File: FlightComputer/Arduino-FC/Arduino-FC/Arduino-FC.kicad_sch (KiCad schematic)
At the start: 5 parts, among them J1 Conn_02x04_Counter_Clockwise, J2 Conn_01x06, J3 Conn_01x07, J4 Conn_01x05, U1 TPS61236PRWLR

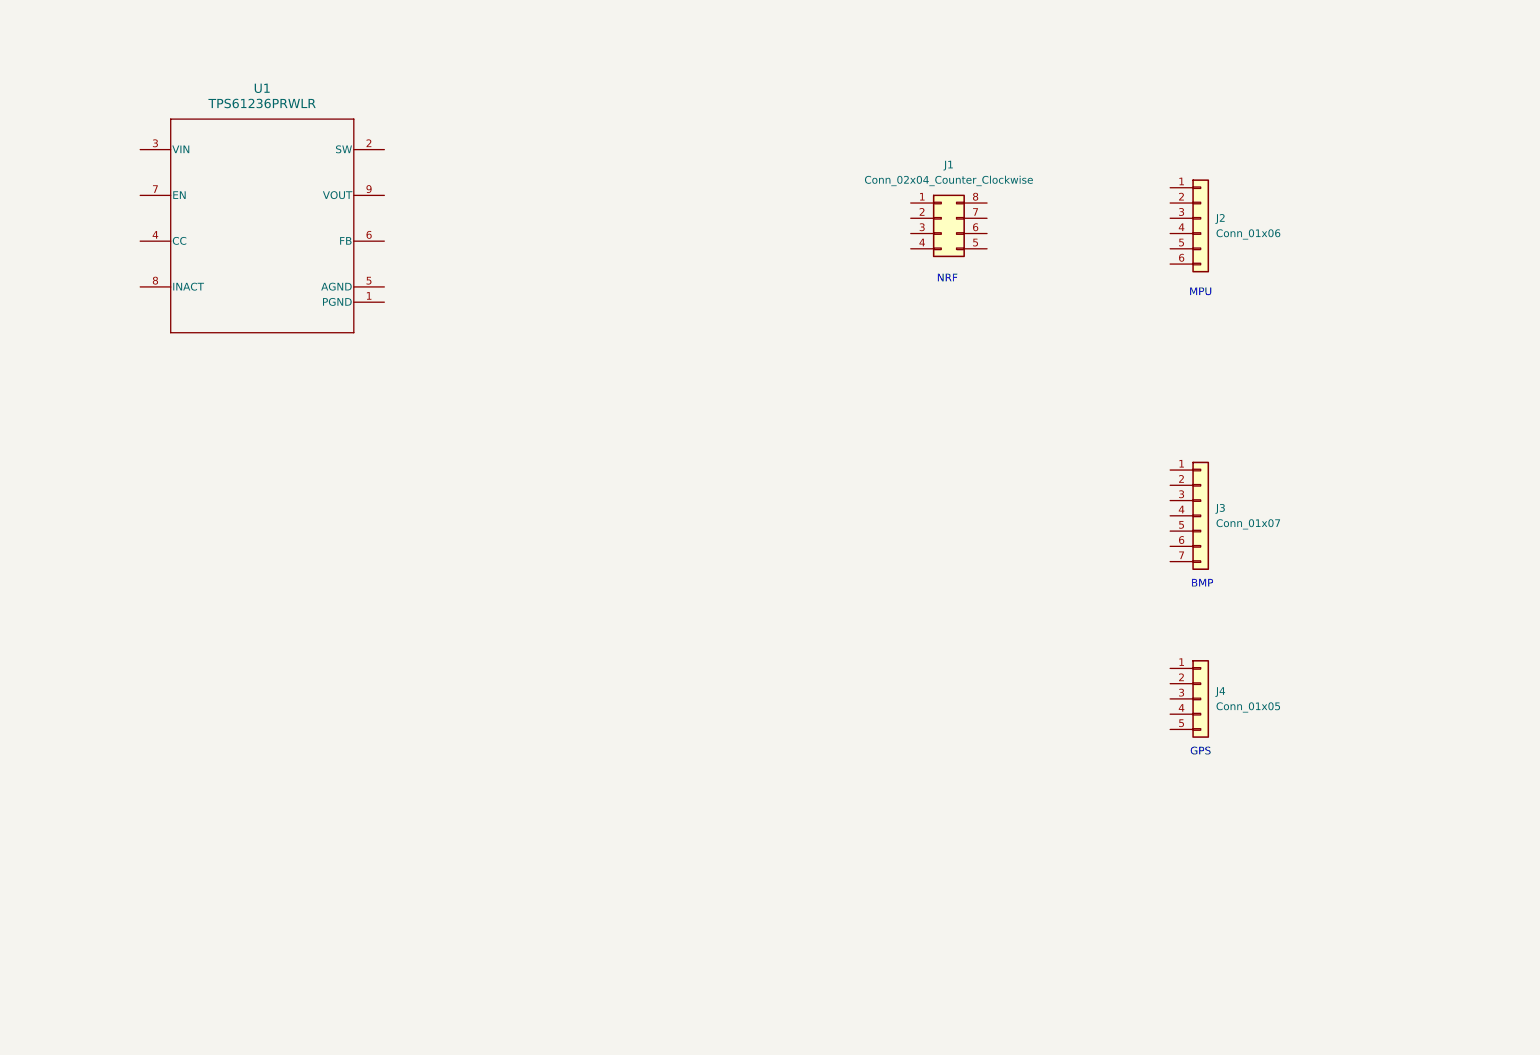
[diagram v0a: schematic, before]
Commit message: Added Main.ino
Updated schematic connections
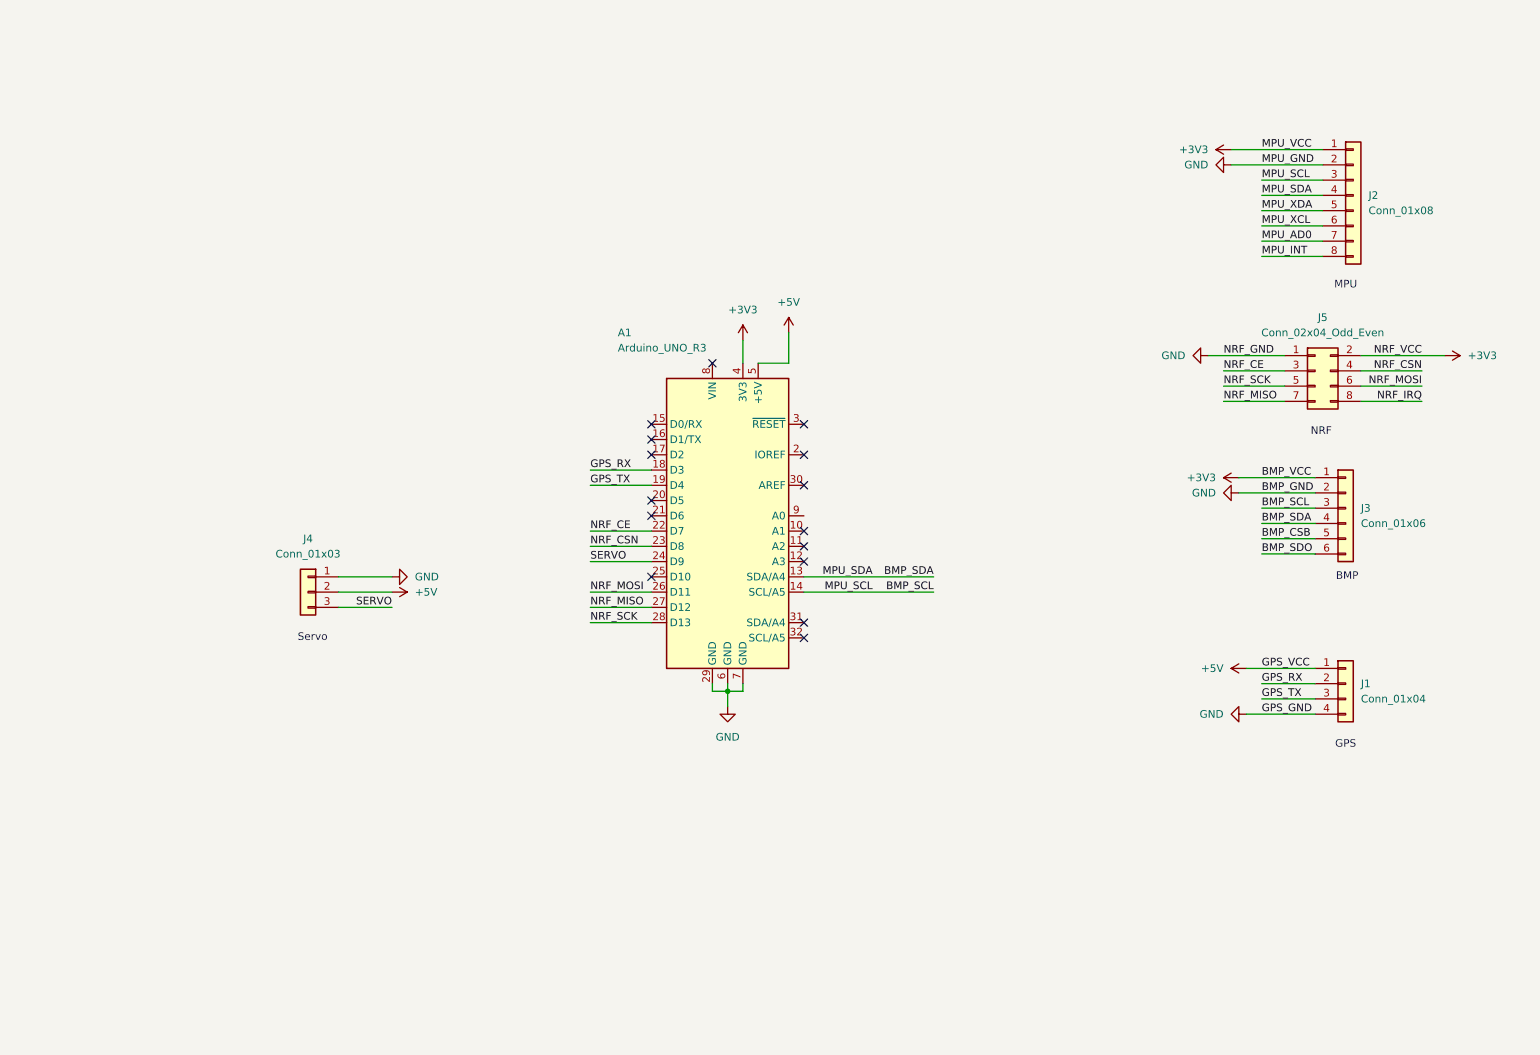
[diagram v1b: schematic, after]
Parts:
- removed J1: Conn_02x04_Counter_Clockwise, symbol Connector_Generic:Conn_02x04_Counter_Clockwise
- removed J2: Conn_01x06, symbol Connector_Generic:Conn_01x06
- removed J3: Conn_01x07, symbol Connector_Generic:Conn_01x07
- removed J4: Conn_01x05, symbol Connector_Generic:Conn_01x05
- removed U1: TPS61236PRWLR, RWL0009A, symbol TPS61236P:TPS61236PRWLR
- added A1: Arduino_UNO_R3, Module:Arduino_UNO_R3, symbol MCU_Module:Arduino_UNO_R3
- added J1: Conn_01x04, symbol Connector_Generic:Conn_01x04
- added J2: Conn_01x08, symbol Connector_Generic:Conn_01x08
- added J3: Conn_01x06, symbol Connector_Generic:Conn_01x06
- added J4: Conn_01x03, symbol Connector_Generic:Conn_01x03
- added J5: Conn_02x04_Odd_Even, symbol Connector_Generic:Conn_02x04_Odd_Even
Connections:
- new net +3V3: A1.4 (3V3), J2.1 (Pin_1), J3.1 (Pin_1), J5.2 (Pin_2)
- new net +5V: A1.5 (+5V), J1.1 (Pin_1), J4.2 (Pin_2)
- new net BMP_CSB: J3.5 (Pin_5)
- new net BMP_SCL: A1.14 (SCL/A5), J2.3 (Pin_3), J3.3 (Pin_3)
- new net BMP_SDA: A1.13 (SDA/A4), J2.4 (Pin_4), J3.4 (Pin_4)
- new net BMP_SDO: J3.6 (Pin_6)
- new net GND: A1.29 (GND), A1.6 (GND), A1.7 (GND), J1.4 (Pin_4), J2.2 (Pin_2), J3.2 (Pin_2), J4.1 (Pin_1), J5.1 (Pin_1)
- new net GPS_RX: A1.18 (D3), J1.2 (Pin_2)
- new net GPS_TX: A1.19 (D4), J1.3 (Pin_3)
- new net MPU_AD0: J2.7 (Pin_7)
- new net MPU_INT: J2.8 (Pin_8)
- new net MPU_XCL: J2.6 (Pin_6)
- new net MPU_XDA: J2.5 (Pin_5)
- new net NRF_CE: A1.22 (D7), J5.3 (Pin_3)
- new net NRF_CSN: A1.23 (D8), J5.4 (Pin_4)
- new net NRF_IRQ: J5.8 (Pin_8)
- new net NRF_MISO: A1.27 (D12), J5.7 (Pin_7)
- new net NRF_MOSI: A1.26 (D11), J5.6 (Pin_6)
- new net NRF_SCK: A1.28 (D13), J5.5 (Pin_5)
- new net SERVO: A1.24 (D9), J4.3 (Pin_3)
- no-connect marks 0 -> 15
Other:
- note added: "Servo"

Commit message: Buck Converter
Footprint assignments
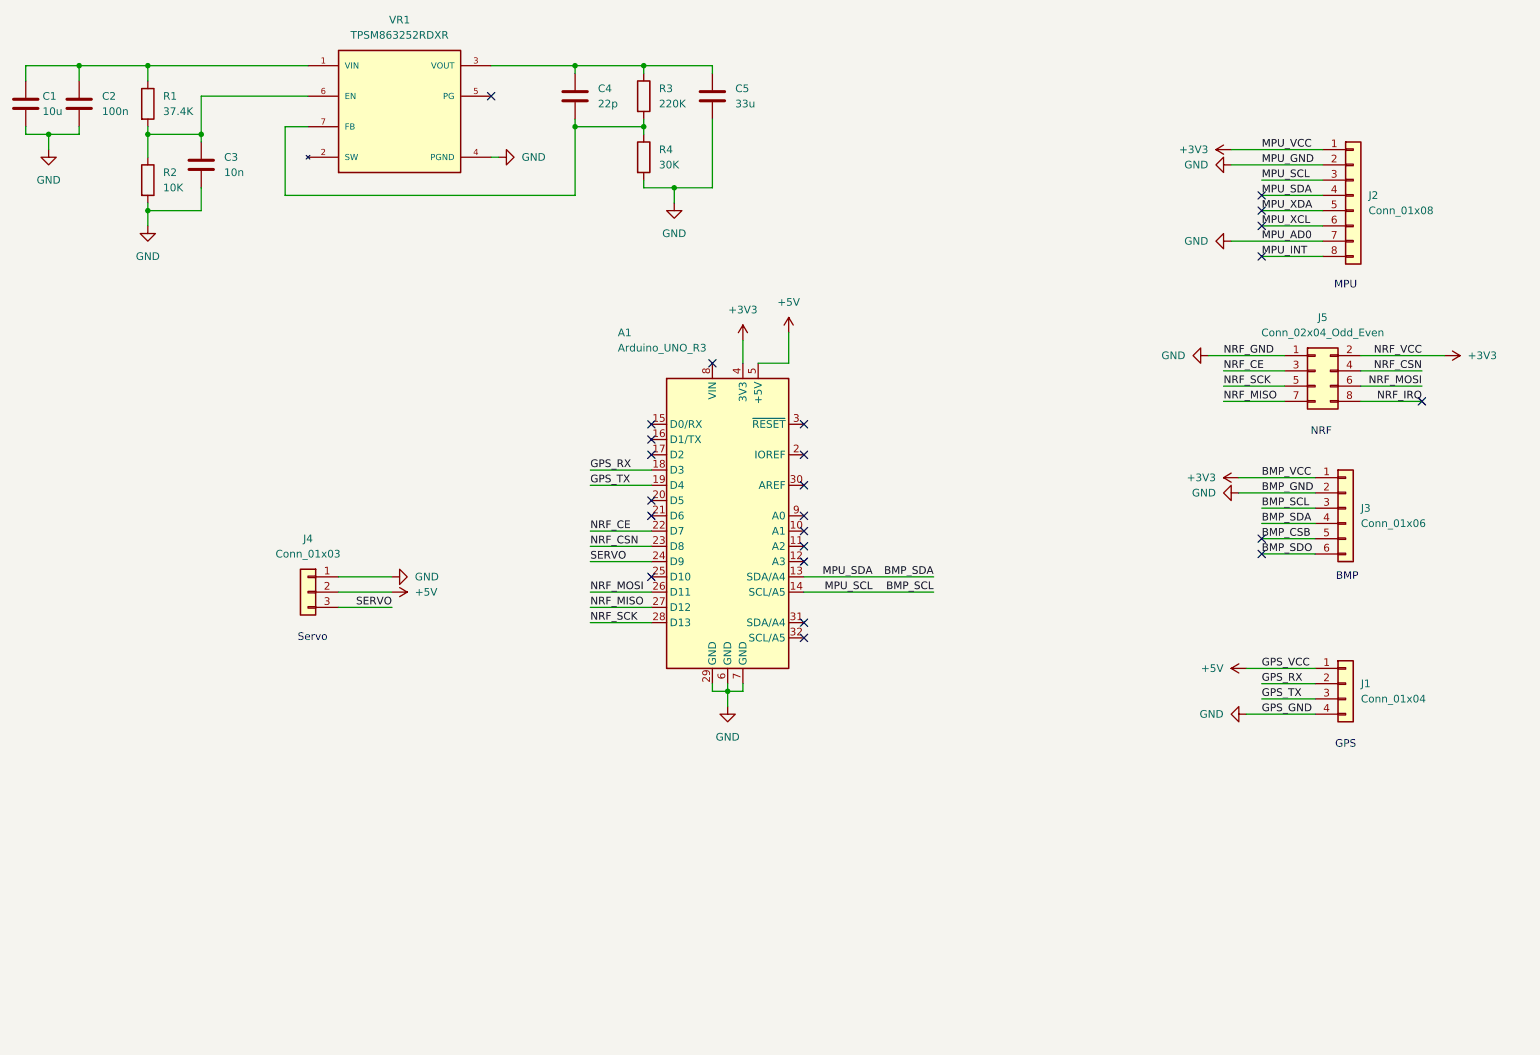
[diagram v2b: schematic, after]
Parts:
- added C1: 10u, Capacitor_SMD:C_0805_2012Metric_Pad1.18x1.45mm_HandSolder, symbol Device:C
- added C2: 100n, Capacitor_SMD:C_0402_1005Metric_Pad0.74x0.62mm_HandSolder, symbol Device:C
- added C3: 10n, Capacitor_SMD:C_0402_1005Metric_Pad0.74x0.62mm_HandSolder, symbol Device:C
- added C4: 22p, Capacitor_SMD:C_0402_1005Metric_Pad0.74x0.62mm_HandSolder, symbol Device:C
- added C5: 33u, Capacitor_SMD:C_1812_4532Metric_Pad1.57x3.40mm_HandSolder, symbol Device:C
- added R1: 37.4K, Resistor_SMD:R_0402_1005Metric_Pad0.72x0.64mm_HandSolder, symbol Device:R
- added R2: 10K, Resistor_SMD:R_0402_1005Metric_Pad0.72x0.64mm_HandSolder, symbol Device:R
- added R3: 220K, Resistor_SMD:R_0603_1608Metric_Pad0.98x0.95mm_HandSolder, symbol Device:R
- added R4: 30K, Resistor_SMD:R_0603_1608Metric_Pad0.98x0.95mm_HandSolder, symbol Device:R
- added VR1: TPSM863252RDXR, TPSM863252RDXR:VREG_TPSM863252RDXR, symbol TPSM863252RDXR:TPSM863252RDXR
- J1: footprint (none) -> Connector_PinHeader_2.54mm:PinHeader_1x04_P2.54mm_Vertical
- J2: footprint (none) -> Connector_PinHeader_2.54mm:PinHeader_1x08_P2.54mm_Vertical
- J3: footprint (none) -> Connector_PinHeader_2.54mm:PinHeader_1x06_P2.54mm_Vertical
- J4: footprint (none) -> Connector_PinHeader_2.54mm:PinHeader_1x03_P2.54mm_Vertical
- J5: footprint (none) -> Connector_PinHeader_2.54mm:PinHeader_2x04_P2.54mm_Vertical
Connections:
- net MPU_AD0 is gone; now on net GND: J2.7 (Pin_7)
- net GND: now also C1.2, C2.2, C3.2, C5.2, R2.2, R4.2, VR1.4 (PGND)
- new net: C1.1, C2.1, R1.1, VR1.1 (VIN)
- new net: C4.1, C5.1, R3.1, VR1.3 (VOUT)
- new net: C3.1, R1.2, R2.1, VR1.6 (EN)
- new net: C4.2, R3.2, R4.1, VR1.7 (FB)
- no-connect marks 15 -> 24

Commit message: Custom NRF Adapter footprint
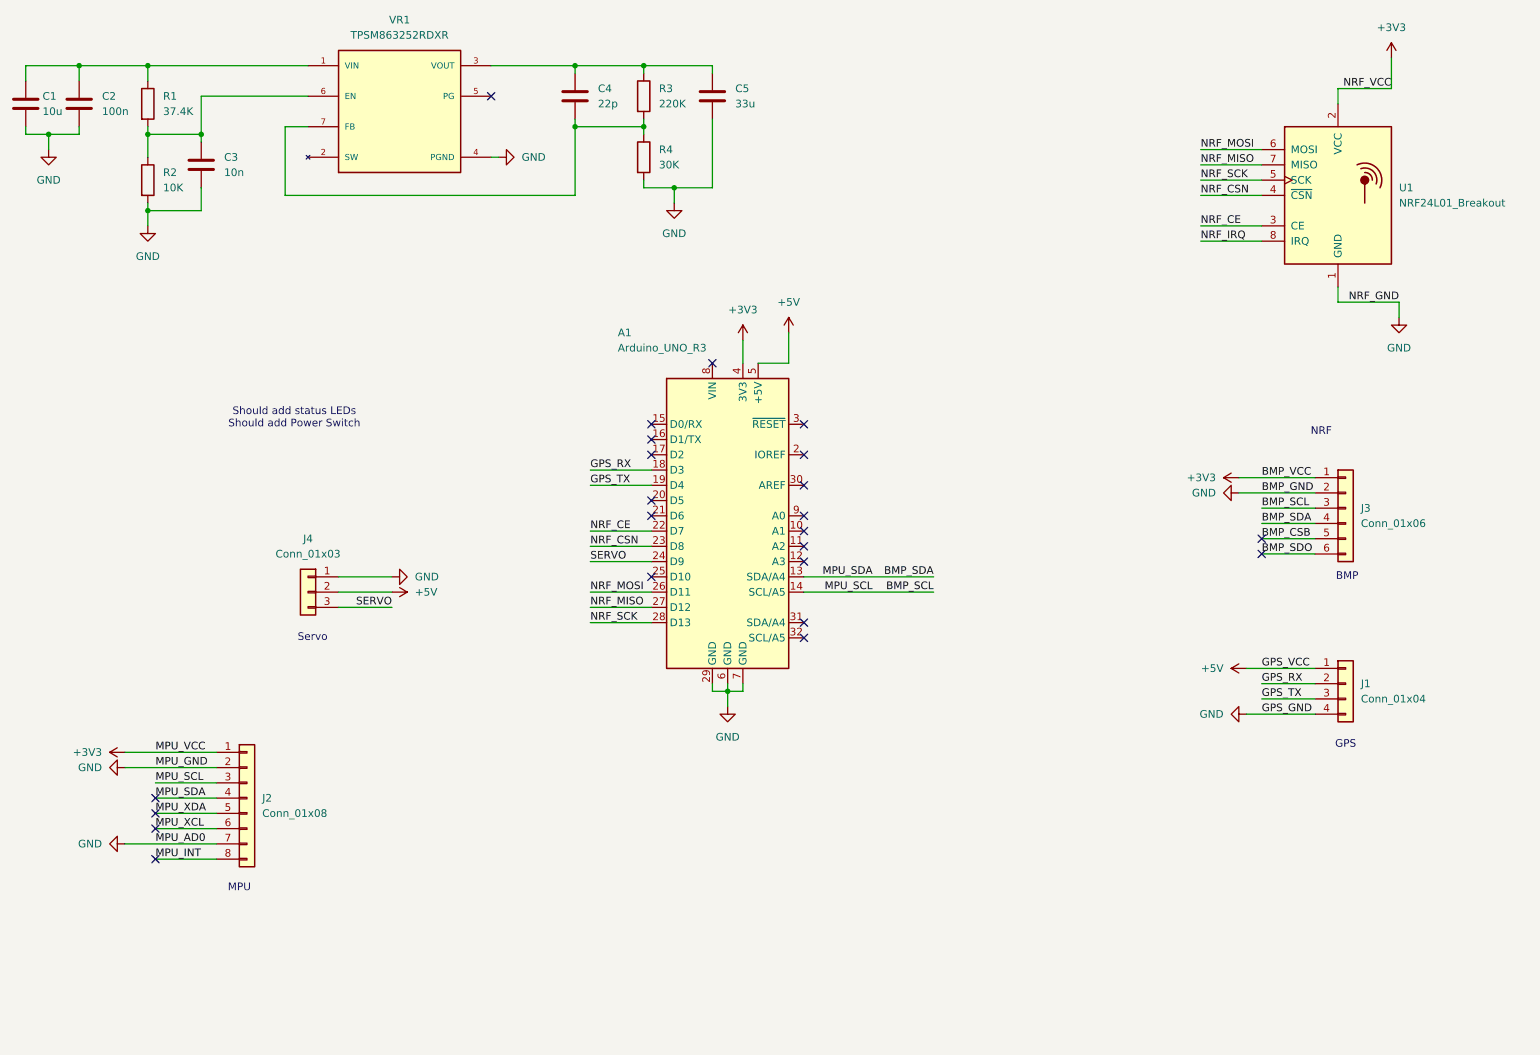
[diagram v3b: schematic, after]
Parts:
- removed J5: Conn_02x04_Odd_Even, Connector_PinHeader_2.54mm:PinHeader_2x04_P2.54mm_Vertical, symbol Connector_Generic:Conn_02x04_Odd_Even
- added U1: NRF24L01_Breakout, RF_Module:nRF24L01_Breakout, symbol RF:NRF24L01_Breakout
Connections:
- net +3V3: now also U1.2 (VCC)
- net GND: now also U1.1 (GND)
- net NRF_CE: now also U1.3 (CE)
- net NRF_CSN: now also U1.4 (~{CSN})
- net NRF_IRQ: now also U1.8 (IRQ)
- net NRF_MISO: now also U1.7 (MISO)
- net NRF_MOSI: now also U1.6 (MOSI)
- net NRF_SCK: now also U1.5 (SCK)
- no-connect marks 24 -> 23
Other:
- note added: "Should add status LEDs Should add Power Switch"
- moved on the sheet: J2

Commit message: Indicator LEDs + Screw terminal
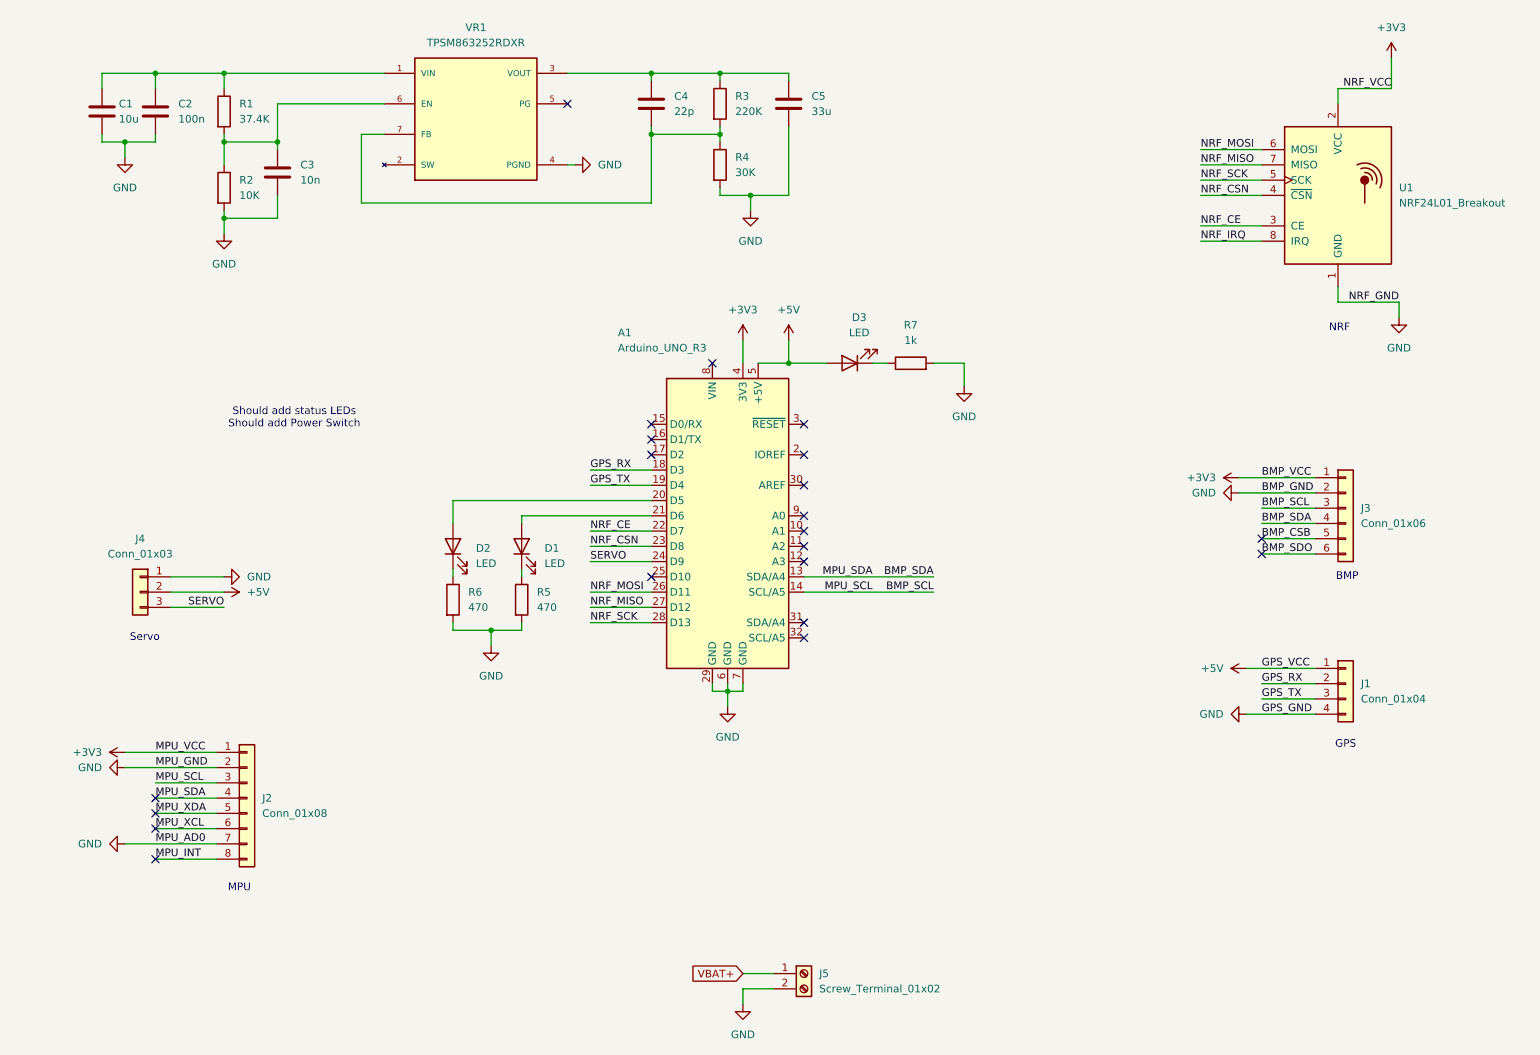
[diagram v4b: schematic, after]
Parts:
- added D1, D2, D3: LED, LED_THT:LED_D5.0mm_Clear, symbol Device:LED
- added J5: Screw_Terminal_01x02, TerminalBlock:TerminalBlock_MaiXu_MX126-5.0-02P_1x02_P5.00mm, symbol Connector:Screw_Terminal_01x02
- added R5, R6: 470, Resistor_THT:R_Axial_DIN0414_L11.9mm_D4.5mm_P15.24mm_Horizontal, symbol Device:R
- added R7: 1k, Resistor_THT:R_Axial_DIN0414_L11.9mm_D4.5mm_P15.24mm_Horizontal, symbol Device:R
- U1: footprint RF_Module:nRF24L01_Breakout -> nRF24L01:nRF24L01-Adapter
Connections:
- net +5V: now also D3.2 (A)
- net GND: now also J5.2 (Pin_2), R5.2, R6.2, R7.2
- net at A1.20 (D5): now also D2.2 (A)
- net at A1.21 (D6): now also D1.2 (A)
- new net: D1.1 (K), R5.1
- new net: D3.1 (K), R7.1
- new net: D2.1 (K), R6.1
- new net VBAT+: J5.1 (Pin_1)
- no-connect marks 23 -> 21
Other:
- moved on the sheet: C1, C2, C3, C4, C5, J4, R1, R2, R3, R4, VR1
